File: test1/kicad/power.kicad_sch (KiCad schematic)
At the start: 17 parts, among them J10 1x2 100mil, J11 1x2 100mil, J12 1x2 100mil, U10 TPS7A8401A, U11 TPS22916

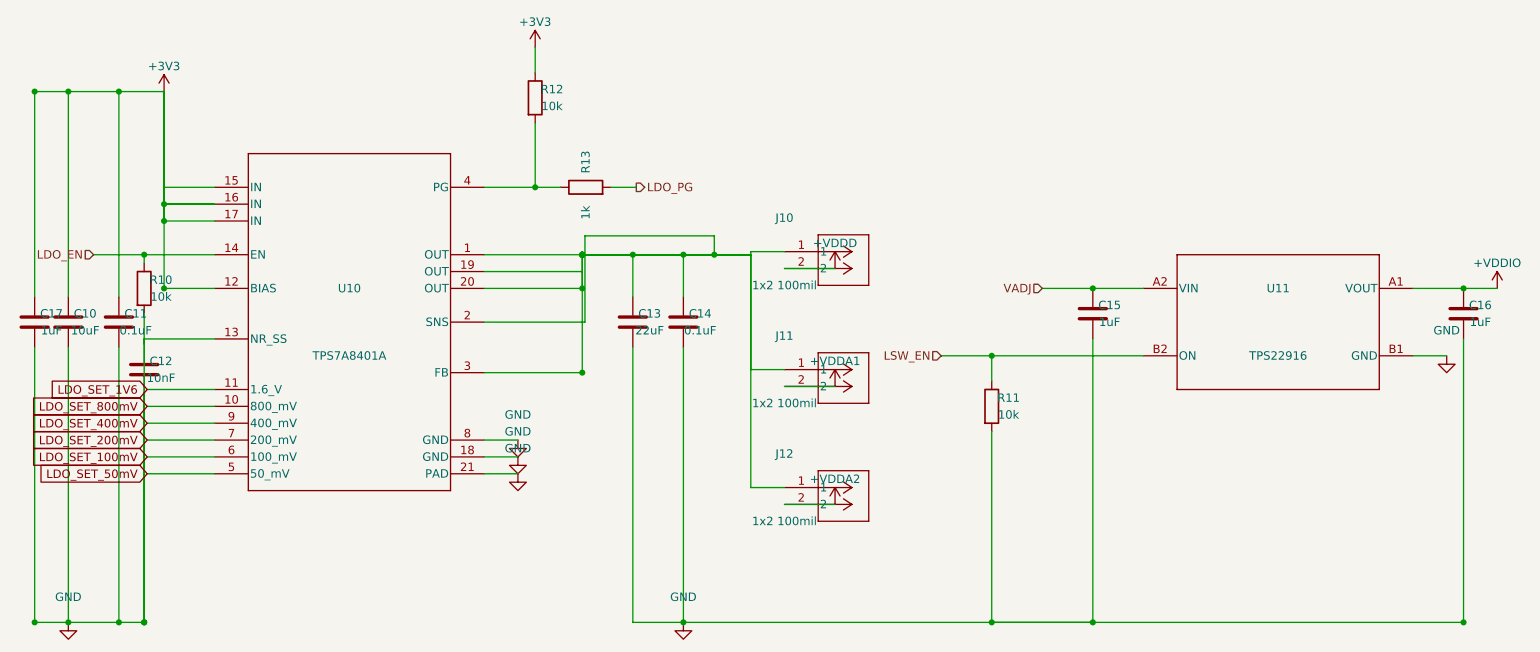
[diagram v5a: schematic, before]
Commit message: Add layout linter + cluster helpers; fix silent shorts across sheets
Introduces gen/layout_lint.py with checks for bbox spacing, wires
through/into a body, parallel-wire overlap on the same axis, bridged
drop columns, and dense GND clusters — non-fatal warnings the strict
validator cannot catch (each net's name is still present in a bridged
component's name set, so per-member name checks pass).

Fixes the bugs the linter exposed:
- FMC routing flipped to exit LEFT (pin-protrusion side) so wires no
  longer pass through the connector body
- bobcat OWT (pins 23-25) + GPIO (37-40) get one drop column per pin,
  ending the silent shorts between adjacent nets
- bobcat SPI pin 14 pull-x shifted off pin 19's column
- bias Q40/Q41 source/drain wires detoured around the body so source
  no longer shorts to drain through the same vertical
- power LDO redundant tap stubs + GND-rail dupes removed; C12 moved
  off R10's column so NR_SS doesn't short to GND
- C11 ↔ R10, J54-56 ↔ R50-52 spacing widened to meet bbox rule

Adds gnd_bus() and decoupling_cluster() helpers in gen/shared.py and
applies gnd_bus() to the eeprom address-strap pins.

Skill doc gets rules for pin-protrusion side, per-pin drop columns,
and same-axis wire overlap. All 7 sheets now pass kicad-cli parse,
the strict connectivity validator, and the layout linter.

Co-Authored-By: Claude Opus 4.7 (1M context) <noreply@anthropic.com>
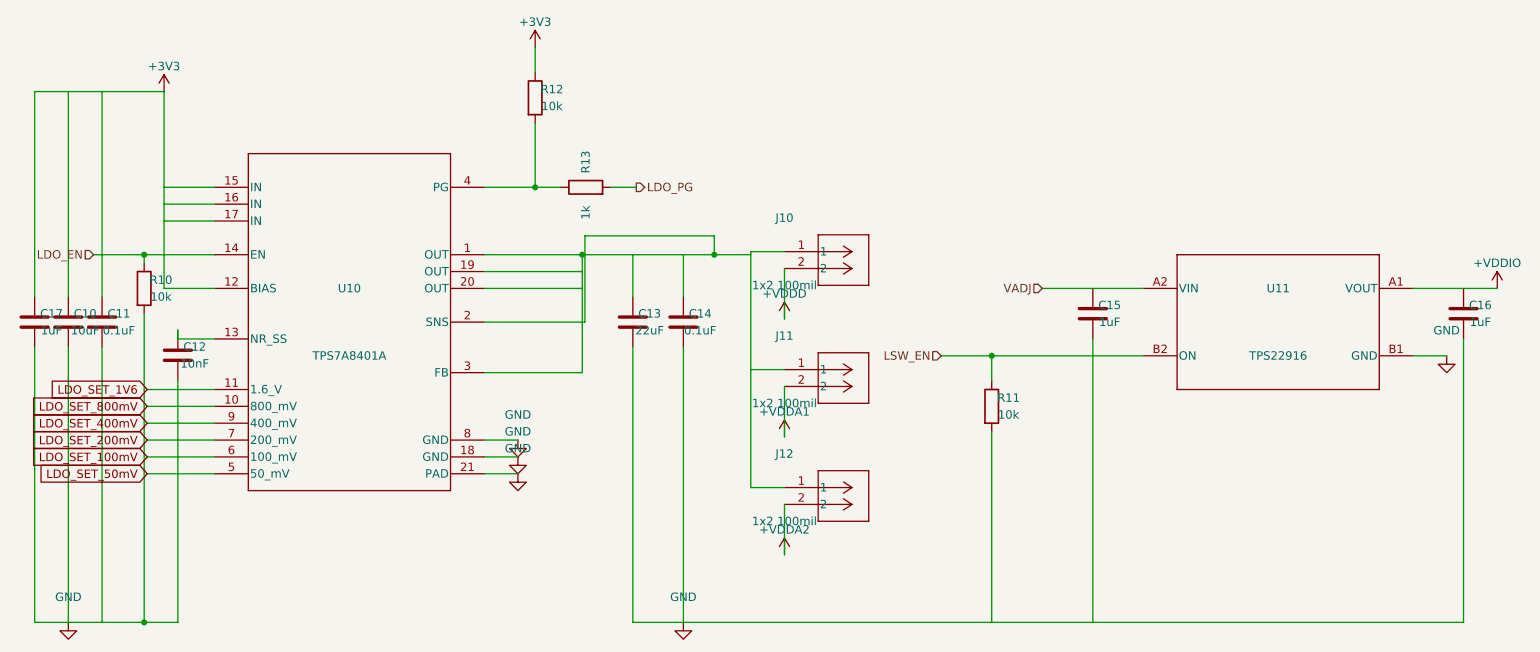
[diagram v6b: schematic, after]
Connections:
- net +3V3: no longer C10.1, C11.1, U10.15 (IN), U10.16 (IN), U10.17 (IN)
- net +VDDIO: no longer C16.1
- net GND: no longer C11.2, C12.1, C12.2, C17.2, R10.2, R11.2, U10.13 (NR_SS)
- net VADJ: no longer C15.1
- new net: C11.2, C12.2, C17.2, R10.2
- new net: U10.1 (OUT), U10.2 (SNS), U10.3 (FB)
- new net: C12.1, U10.13 (NR_SS)
- new net: J10.1, J12.1
- now unconnected: C13.1, C14.1, J11.1, U10.20 (OUT)
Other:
- moved on the sheet: C11, C12
